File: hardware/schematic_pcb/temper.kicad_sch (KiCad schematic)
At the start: 48 parts, among them J1 conn_01x03, J10 conn_01x05, J11 Conn_01x10, J12 2.54mm Plugin Gold 7P Brass S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, J2 conn_01x03, J3 conn_01x03, J4 conn_01x03, J5 Charge Connector, J6 Conn_01x20, J7 Conn_01x20, J8 conn_01x05, J9 conn_01x05, M1 DMP3099L-7, M2 DMP3099L-7, Q1 2N7002, SW1 Factory Reset, SW2 Reset, SW3 ON/OFF, U1 SPI ROTARY ENCODER, U2 MCP9700, U3 Pico_W, U4 TL431DBZ

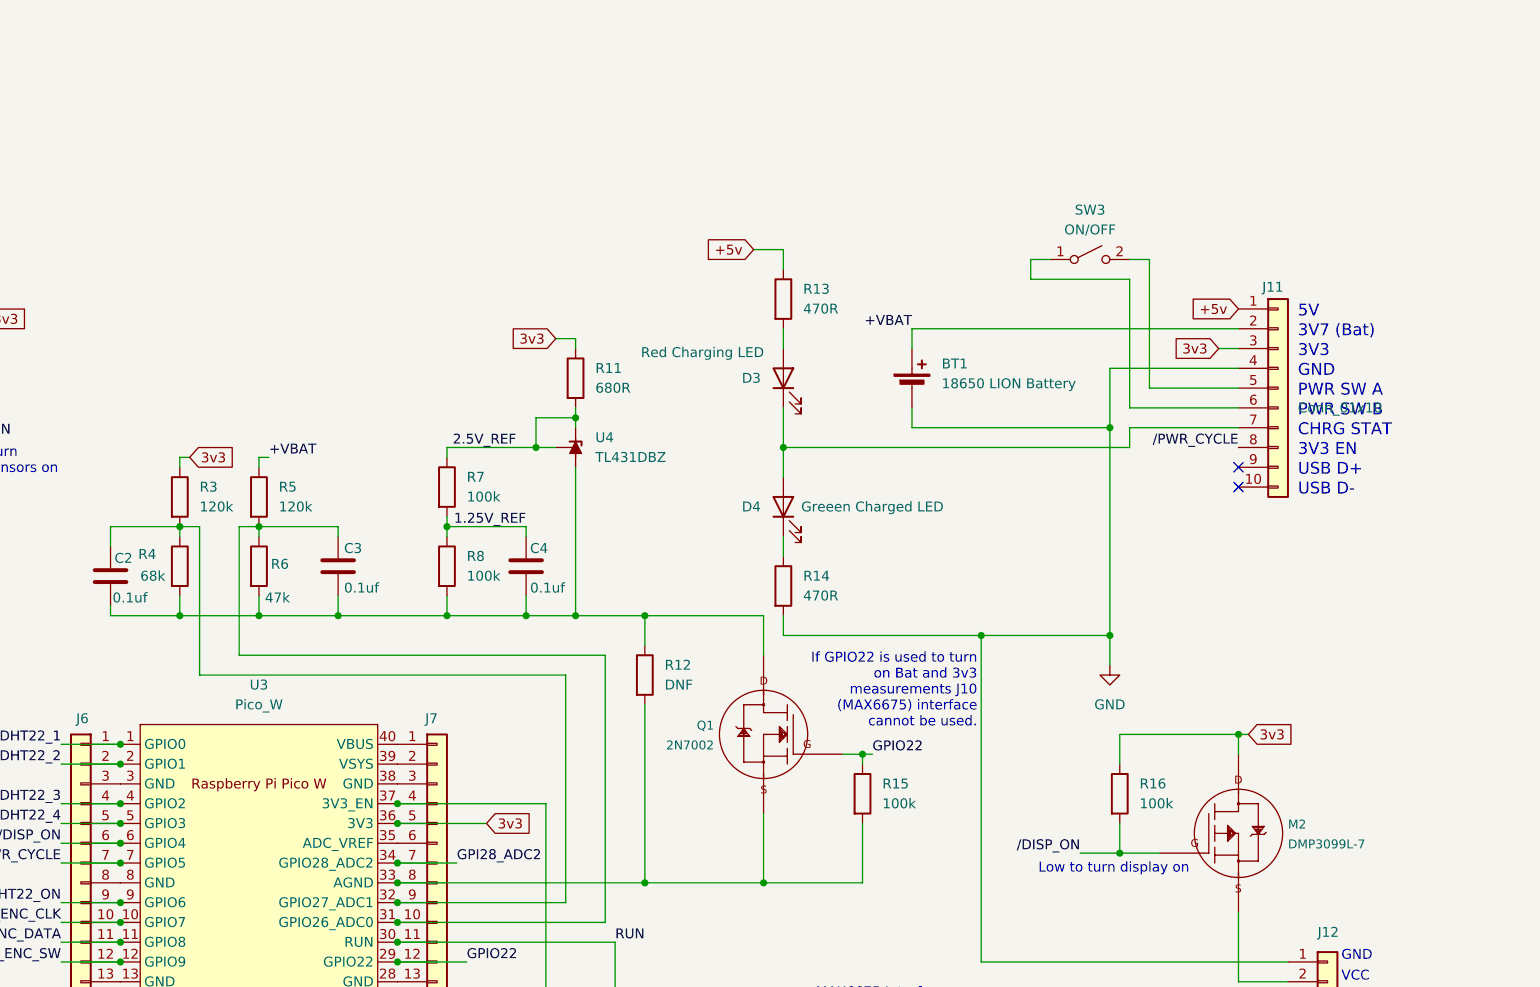
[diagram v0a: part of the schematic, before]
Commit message: First PCB using RPi Pico working
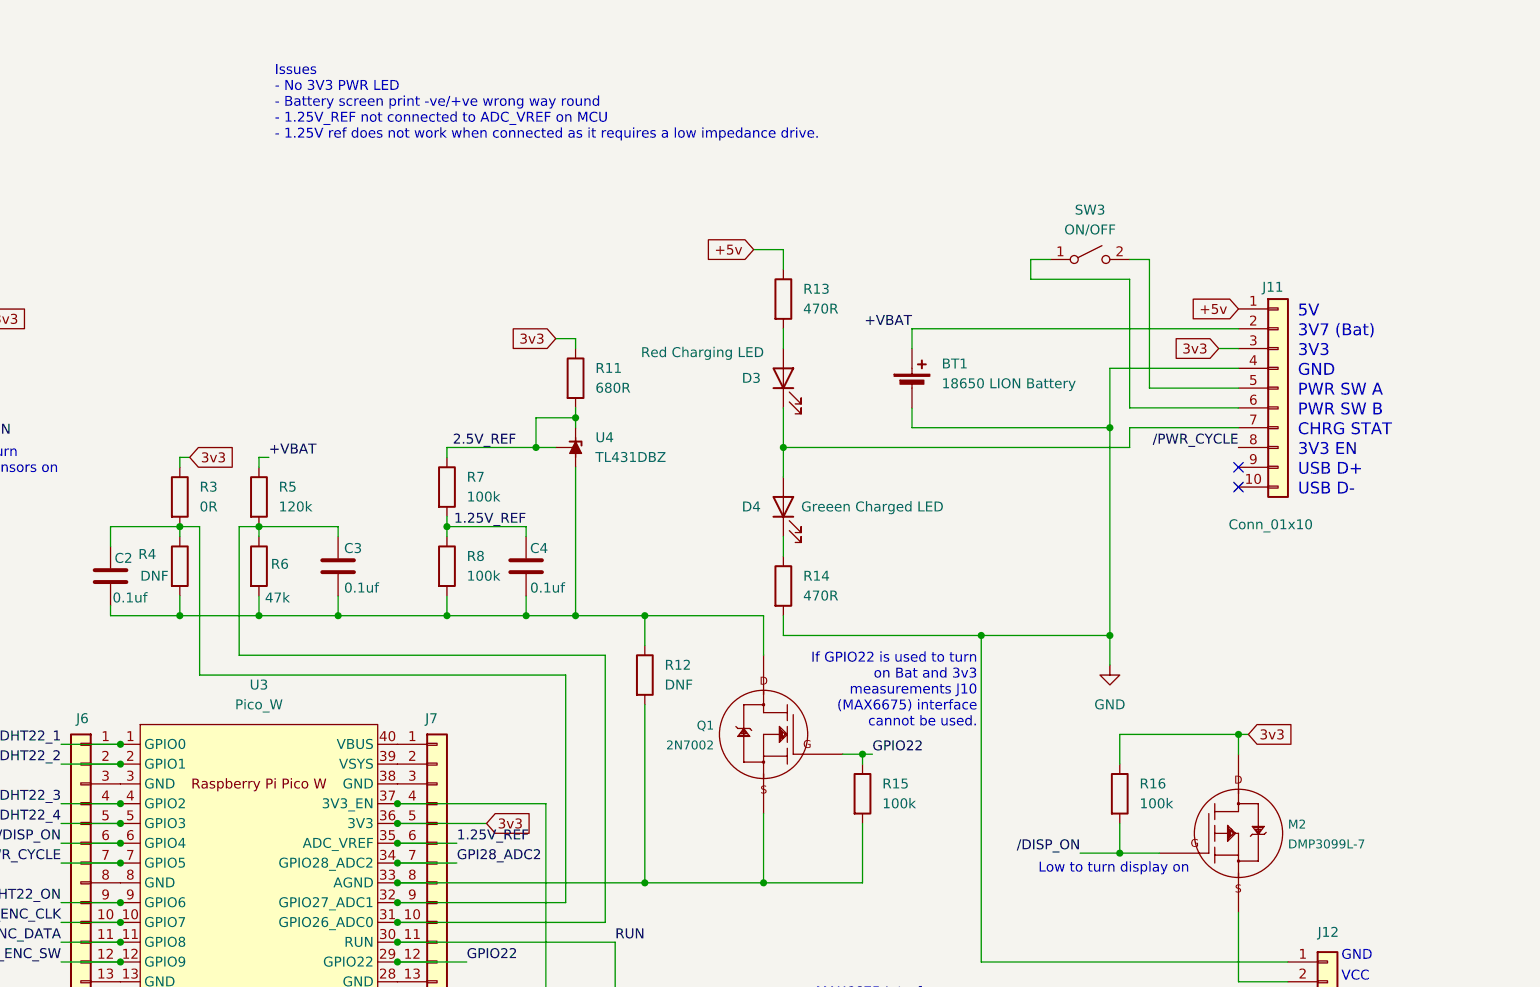
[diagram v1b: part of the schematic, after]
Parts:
- R3: value 120k -> 0R
- R4: value 68k -> DNF
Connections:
- net 1.25V_REF: now also J7.6 (Pin_6), U3.35 (ADC_VREF)
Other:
- note added: "Issues - No 3V3 PWR LED - Battery screen print -ve/+ve wrong way round - 1.25V_REF not connected to ADC_VREF on MCU - 1.25V ref does not work when connected as it requires a low impedance drive."
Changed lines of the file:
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@@
 	)
 	(junction
+		(at 134.62 119.38)
+		(diameter 0)
+		(color 0 0 0 0)
+	)
+	(junction
 		(at 157.48 64.77)
 		(diameter 0)
@@
 	(wire
 		(pts
+			(xy 134.62 119.38) (xy 142.24 119.38)
+		)
+		(stroke
+			(width 0)
+			(type default)
+		)
+	)
+	(wire
+		(pts
 			(xy 41.91 27.94) (xy 52.07 27.94)
 		)
@@
 		)
 	)
+	(text "Issues\n- No 3V3 PWR LED\n- Battery screen print -ve/+ve wrong way round\n- 1.25V_REF not connected to ADC_VREF on MCU\n- 1.25V ref does not work when connected as it requires a low impedance drive."
+		(exclude_from_sim no)
+		(at 118.872 24.384 0)
+		(effects
+			(font
+				(size 1.27 1.27)
+			)
+			(justify left)
+		)
+	)
 	(text "GND"
 		(exclude_from_sim no)
@@
 		)
 	)
+	(label "1.25V_REF"
+		(at 142.24 119.38 0)
+		(effects
+			(font
+				(size 1.27 1.27)
+			)
+			(justify left bottom)
+		)
+	)
 	(label "GPIO16"
 		(at 143.51 154.94 0)
@@
 			)
 		)
-		(property "Value" "120k"
+		(property "Value" "0R"
 			(at 109.22 76.1999 0)
 			(effects
@@
 			)
 		)
-		(property "Value" "68k"
+		(property "Value" "DNF"
 			(at 101.6 85.09 0)
 			(effects
@@
 		)
 		(property "Value" "Conn_01x10"
-			(at 250.19 63.4999 0)
+			(at 241.3 78.486 0)
 			(effects
 				(font

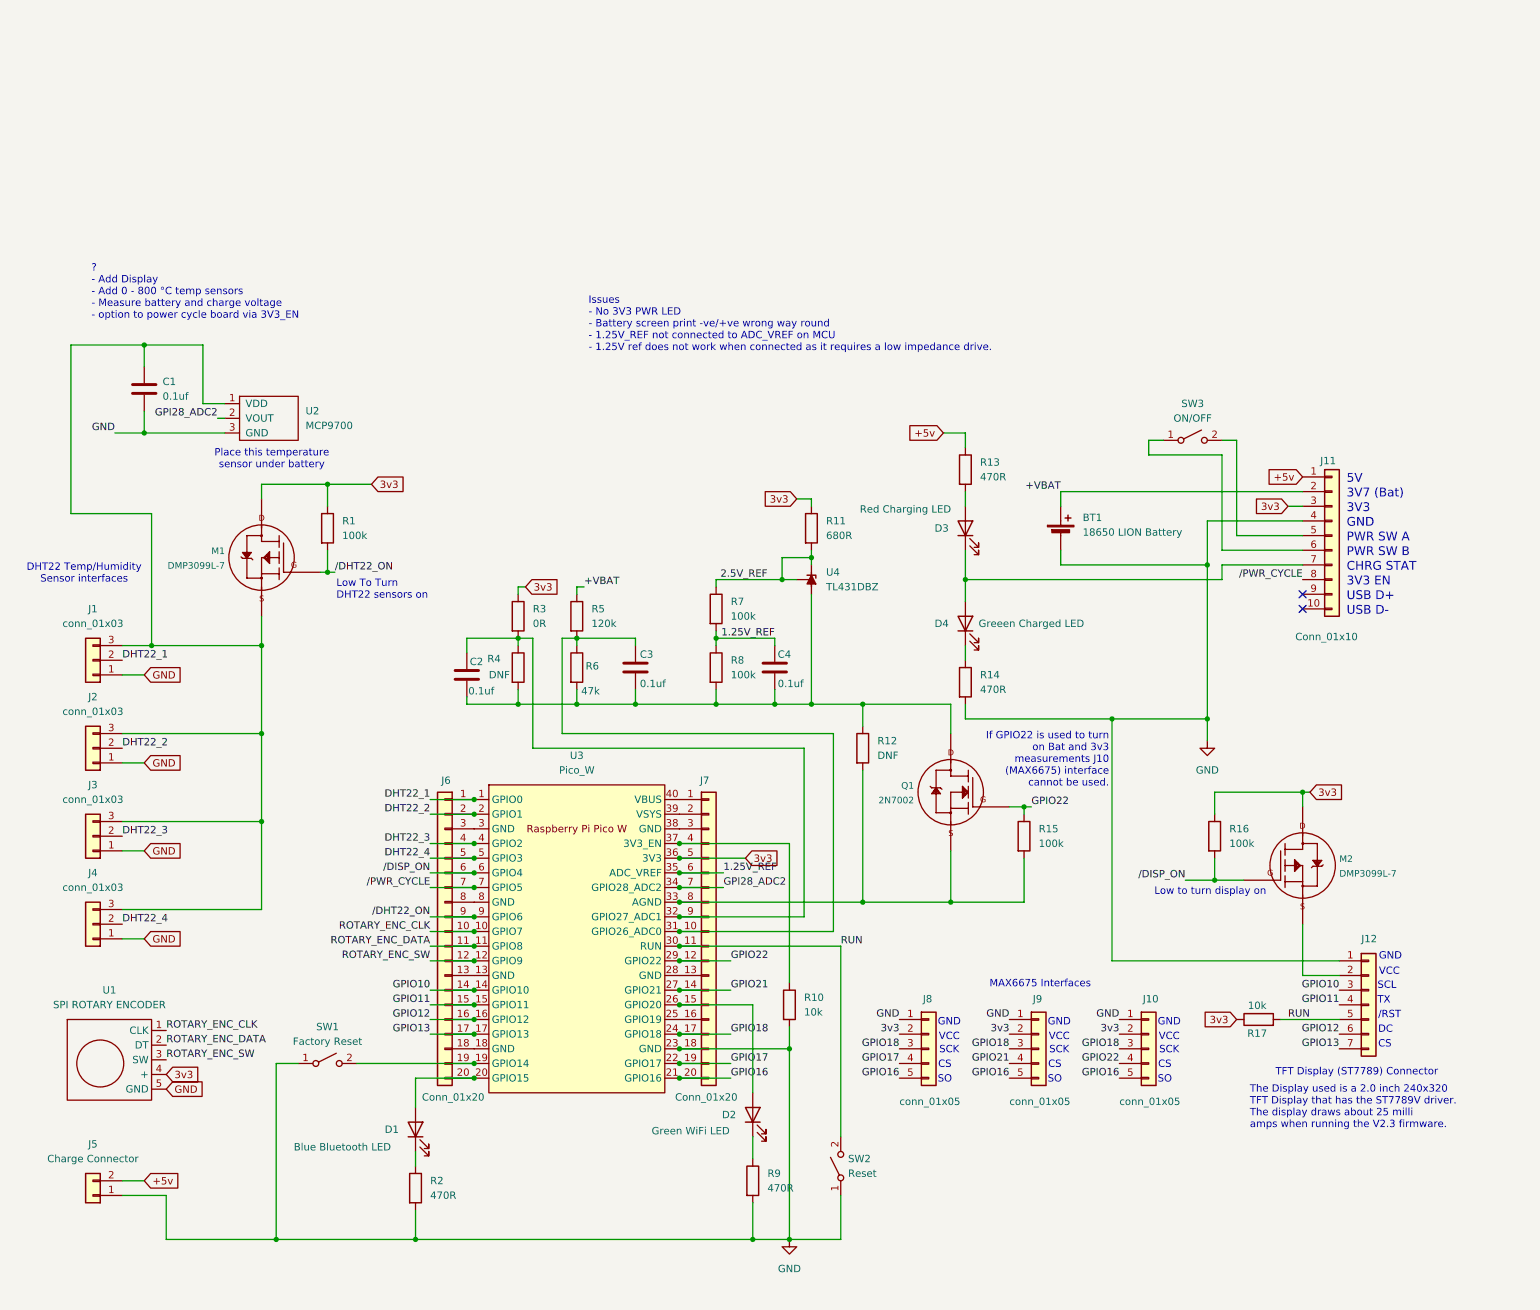
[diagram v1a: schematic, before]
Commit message: V1.2 using an ESP32 rather than a RPi Pico W. The ESP32 can handle low power modes better than the RPi Pico W.
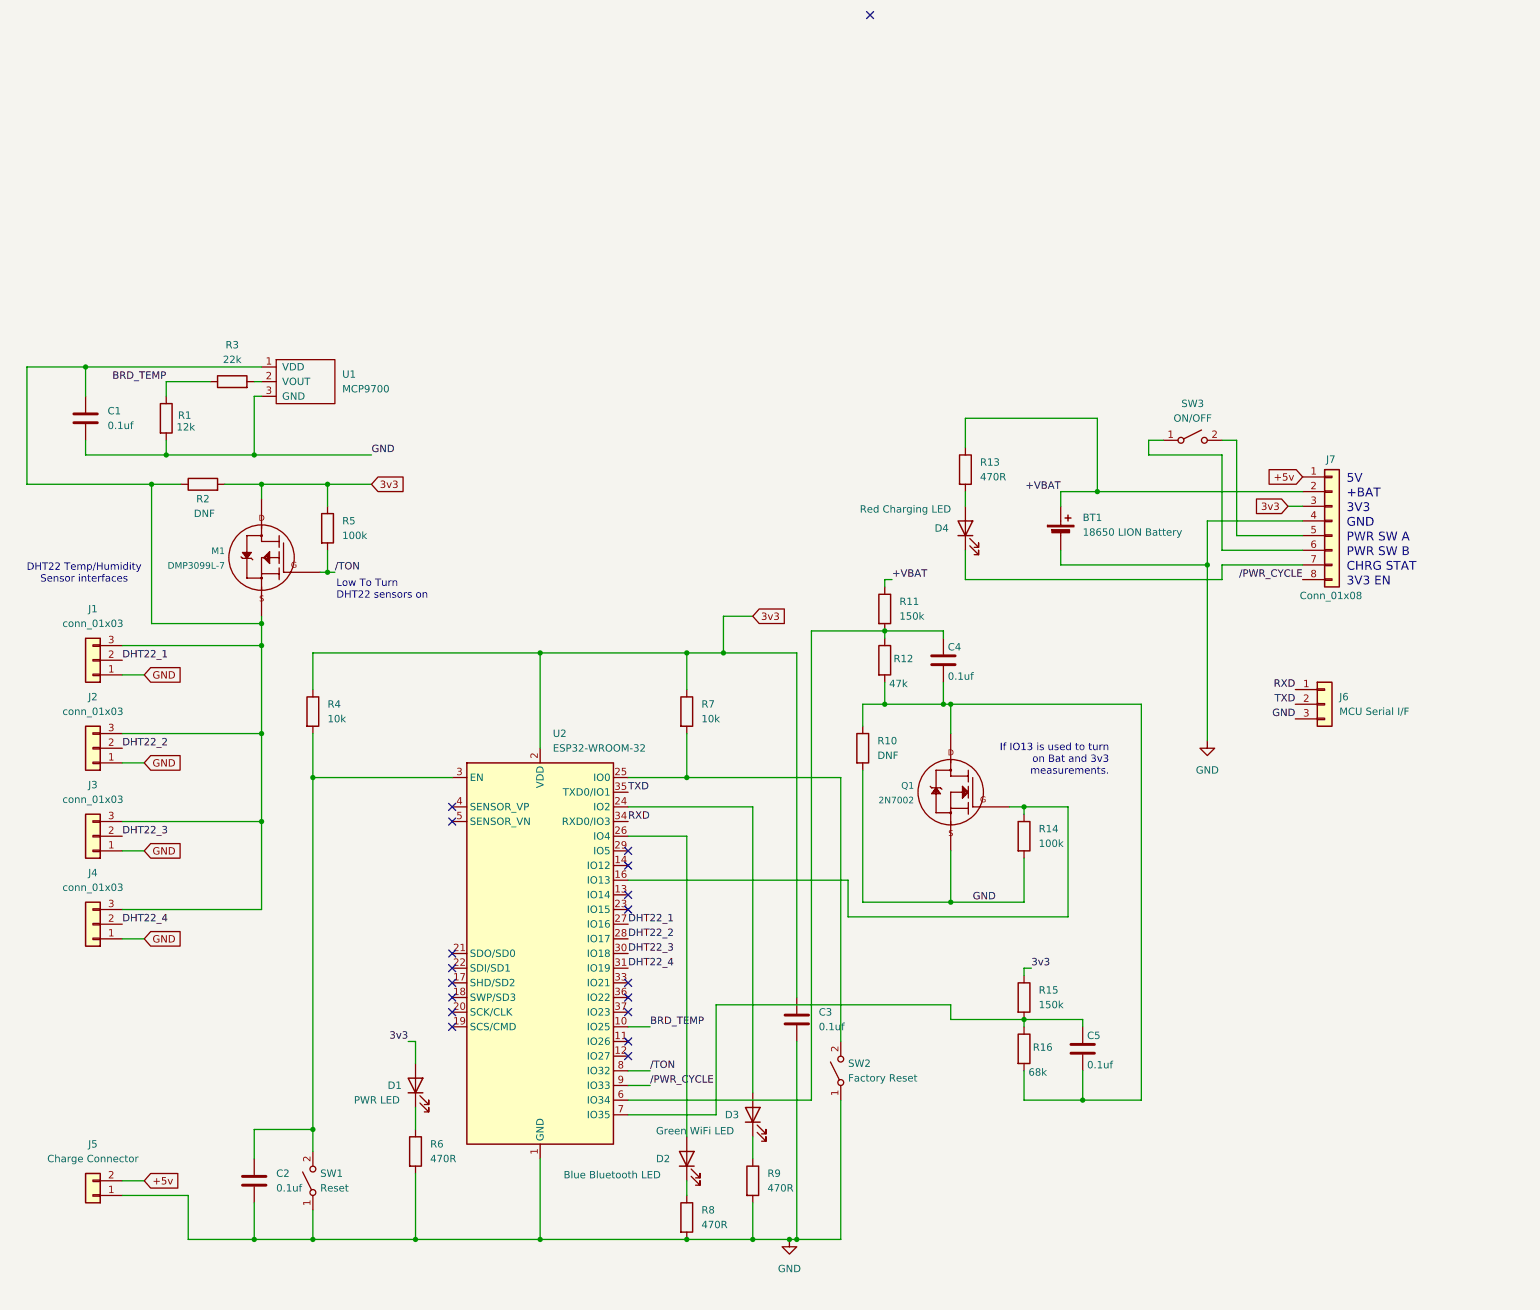
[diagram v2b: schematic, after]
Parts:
- removed C4: 0.1uf, Capacitor_SMD:C_0603_1608Metric, symbol Device:C
- removed D4: Greeen Charged LED, LED_SMD:LED_1206_3216Metric, symbol Device:LED
- removed J10, J8, J9: conn_01x05, Connector_PinHeader_2.54mm:PinHeader_1x05_P2.54mm_Vertical, symbol Connector_Generic:Conn_01x05
- removed J11: Conn_01x10, Connector_PinHeader_2.54mm:PinHeader_1x10_P2.54mm_Vertical, symbol Connector_Generic:Conn_01x10
- removed J12: 2.54mm Plugin Gold 7P Brass Straight 1x7P Plugin,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, Connector_PinHeader_2.54mm:PinHeader_1x07_P2.54mm_Vertical, symbol Connector_Generic:Conn_01x07
- removed J6, J7: Conn_01x20, Connector_PinHeader_2.54mm:PinHeader_1x20_P2.54mm_Vertical, symbol Connector_Generic:Conn_01x20
- removed M2: DMP3099L-7, Package_TO_SOT_SMD:SOT-23-3, symbol pja_1:DMP3099L-7
- removed R10: 10k, Resistor_SMD:R_0603_1608Metric_Pad0.98x0.95mm_HandSolder, symbol Device:R
- removed R11: 680R, Resistor_SMD:R_0603_1608Metric_Pad0.98x0.95mm_HandSolder, symbol Device:R
- removed R14: 470R, Resistor_SMD:R_0603_1608Metric_Pad0.98x0.95mm_HandSolder, symbol Device:R
- removed R17: 10k, Resistor_SMD:R_0603_1608Metric, symbol Device:R
- removed R8: 100k, Resistor_SMD:R_0603_1608Metric_Pad0.98x0.95mm_HandSolder, symbol Device:R
- removed SW2: Reset, PJA_Switches:switch_SPST_5mmx3mmx2.5mm, symbol Switch:SW_SPST
- removed U1: SPI ROTARY ENCODER, Connector_PinHeader_2.54mm:PinHeader_1x05_P2.54mm_Vertical, symbol pja1:SPI_ROTARY_ENCODER
- removed U2: MCP9700, Package_TO_SOT_SMD:SOT-23, symbol pja_1:MCP9700
- removed U3: Pico_W, PJA_RP_pico:RPi_Pico_SMD_TH, symbol RPI Pico:Pico_W
- removed U4: TL431DBZ, Package_TO_SOT_SMD:SOT-23, symbol Reference_Voltage:TL431DBZ
- added C3, C5: 0.1uf, Capacitor_SMD:C_0603_1608Metric, symbol Device:C
- added D1: PWR LED, LED_SMD:LED_1206_3216Metric, symbol Device:LED
- added J6: MCU Serial I/F, Connector_JST:JST_EH_B3B-EH-A_1x03_P2.50mm_Vertical, symbol Connector_Generic:Conn_01x03
- added J7: Conn_01x08, Connector_PinHeader_2.54mm:PinHeader_1x08_P2.54mm_Vertical, symbol Connector_Generic:Conn_01x08
- added R1: 12k, Resistor_SMD:R_0603_1608Metric_Pad0.98x0.95mm_HandSolder, symbol Device:R
- added R15: 150k, Resistor_SMD:R_0603_1608Metric_Pad0.98x0.95mm_HandSolder, symbol Device:R
- added R2: DNF, Resistor_SMD:R_0603_1608Metric_Pad0.98x0.95mm_HandSolder, symbol Device:R
- added R6: 470R, Resistor_SMD:R_0603_1608Metric_Pad0.98x0.95mm_HandSolder, symbol Device:R
- added SW1: Reset, PJA_Switches:switch_SPST_5mmx3mmx2.5mm, symbol Switch:SW_SPST
- added U1: MCP9700, Package_TO_SOT_SMD:SOT-23-3, symbol pja_1:MCP9700
- added U2: ESP32-WROOM-32, PJA_ESP32-footprints-Lib:ESP32-WROOM-32, symbol RF_Module:ESP32-WROOM-32
- R11: renamed from R5; value 120k -> 150k
- R16: value 100k -> 68k
- R3: value 0R -> 22k
- R4: value DNF -> 10k
- R7: value 100k -> 10k
- renumbered C3 to C4, D1 to D2, D2 to D3, D3 to D4, R12 to R10, R6 to R12, R15 to R14, R1 to R5, R2 to R8, SW1 to SW2
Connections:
- net 1.25V_REF is gone; now on an unnamed net: R7.2
- net 2.5V_REF is gone; now on net 3v3: R7.1
- net /DISP_ON is gone; now on an unnamed net: R16.2
- net +5v: now also J7.1 (Pin_1); no longer R13.1
- net +VBAT: now also R13.1, J7.2 (Pin_2)
- net 3v3: now also R4.1, C3.1, D1.2 (A), J7.3 (Pin_3), R15.1, R2.2, U2.2 (VDD); no longer R16.1, R3.1
- net DHT22_1: now also U2.27 (IO16)
- net DHT22_2: now also U2.28 (IO17)
- net DHT22_3: now also U2.30 (IO18)
- net DHT22_4: now also U2.31 (IO19)
- net GND: now also C2.2, Q1.2 (S), R10.2, R14.2, C3.2, J6.3 (Pin_3), J7.4 (Pin_4), R1.2, R6.2, SW1.1 (A), U1.3 (GND), U2.1 (GND), U2.15 (GND), U2.38 (GND), U2.39 (GND)
- net /PWR_CYCLE: now also J7.8 (Pin_8), U2.9 (IO33)
- net at C4.1, R11.2, R12.1: now also U2.6 (IO34)
- net at C4.2, Q1.3 (D), R10.1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: now also C5.2; no longer C2.2, R4.2
- net at SW2.2 (B): now also U2.25 (IO0)
- net at D2.2 (A): now also U2.26 (IO4)
- net at D4.1 (K): now also J7.7 (Pin_7)
- net at C1.1, J1.3 (Pin_3), J2.3 (Pin_3)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: now also R2.1, U1.1 (VDD)
- net at D3.2 (A): now also U2.24 (IO2)
- net at SW3.1 (A): now also J7.6 (Pin_6)
- net at SW3.2 (B): now also J7.5 (Pin_5)
- net GPIO22: no longer names the net of Q1.1 (G), R14.1
- net GPIO22: now also U2.16 (IO13)
- net /DHT22_ON renamed /TON
- net /TON: now also U2.8 (IO32)
- new net: C5.1, R15.2, R16.1, U2.7 (IO35)
- new net: C2.1, R4.2, SW1.2 (B), U2.3 (EN)
- new net: D1.1 (K), R6.1
- new net: R3.2, U1.2 (VOUT)
- new net BRD_TEMP: R1.1, R3.1, U2.10 (IO25)
- new net RXD: J6.1 (Pin_1), U2.34 (RXD0/IO3)
- new net TXD: J6.2 (Pin_2), U2.35 (TXD0/IO1)
- no-connect marks 2 -> 18
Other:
- note added: "+BAT"
- note added: "If IO13 is used to turn on Bat and 3v3 measurements."
- note removed: "/RST"
- note removed: "3V7 (Bat)"
- note removed: "? - Add Display - Add 0 - 800 °C temp sensors - Measure battery and charge voltage - option to power cycle board via 3V3_EN"
- note removed: "CS"
- note removed: "DC"
- note removed: "If GPIO22 is used to turn on Bat and 3v3 measurements J10 (MAX6675) interface cannot be used."
- note removed: "Issues - No 3V3 PWR LED - Battery screen print -ve/+ve wrong way round - 1.25V_REF not connected to ADC_VREF on MCU - 1.25V ref does not work when connected as it requires a low impedance drive."
- note removed: "Low to turn display on"
- note removed: "MAX6675 Interfaces"
- note removed: "Place this temperature sensor under battery"
- note removed: "SCK"
- note removed: "SCL"
- note removed: "SO"
- note removed: "TFT Display (ST7789) Connector"
- note removed: "TX"
- note removed: "The Display used is a 2.0 inch 240x320 TFT Display that has the ST7789V driver. The display draws about 25 milli amps when running the V2.3 firmware."
- note removed: "USB D+"
- note removed: "USB D-"
- note removed: "VCC"
- moved on the sheet: C4, D2, R11, R12, R8, SW2
